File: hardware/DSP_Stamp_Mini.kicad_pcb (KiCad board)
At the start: 2 copper layers, 37.5 x 62 mm, 73 parts, among them J1 Conn_01x10, J2 SM03B-SRSS-TB, J3 Conn_01x05, J4 USB_C_Receptacle_USB2.0_14P, J6 Conn_01x10, J7 Conn_01x02, J8 Conn_01x04, SW1 SW_Push, SW2 SW_Push, U1 RP2350_80QFN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

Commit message: repo cleanup
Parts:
- removed J3: Conn_01x05, Connector_PinHeader_2.54mm:PinHeader_1x05_P2.54mm_Vertical_SMD_Pin1Right
- removed J6: Conn_01x10, Connector_PinHeader_2.54mm:PinHeader_1x10_P2.54mm_Vertical_SMD_Pin1Right
- removed J7: Conn_01x02, Connector_PinHeader_2.54mm:PinHeader_1x02_P2.54mm_Vertical_SMD_Pin1Right
- added J5: Conn_01x12, Connector_PinHeader_2.54mm:PinHeader_1x12_P2.54mm_Vertical, B.Cu at (93.8, 63.5)
- J1: value Conn_01x10 -> Conn_01x14; footprint Connector_PinHeader_2.54mm:PinHeader_1x10_P2.54mm_Vertical_SMD_Pin1Right -> Connector_PinHeader_2.54mm:PinHeader_1x14_P2.54mm_Vertical
- moved U6 35.7 mm to (117.5, 65.0)
- moved C26 35.7 mm to (121.1, 66.4)
- moved C27 35.7 mm to (114.1, 66.4)
- moved C28 35.7 mm to (123.1, 66.4)
- moved C29 35.7 mm to (112.1, 66.4)
- moved C30 35.7 mm to (125.1, 66.4)
- moved J1 19.9 mm to (129.3, 63.5), turned to 180 degrees
- moved R19 14.2 mm to (100.0, 99.9), turned to 90 degrees
- moved C21 13.7 mm to (121.0, 87.0), turned to -90 degrees
- moved D3 13.6 mm to (101.5, 99.9), turned to 90 degrees
- moved R18 13.6 mm to (104.5, 99.9), turned to 90 degrees
- moved D2 13.4 mm to (103.0, 99.9), turned to 90 degrees
- moved R13 12.0 mm to (125.5, 74.0), turned to 90 degrees
- moved D1 8.46 mm to (118.5, 59.5)
- moved R16 8.46 mm to (117.0, 59.5)
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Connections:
- J1 pad 2: /GPIO40_ADC0 -> /GPIO47_ADC7
- J1 pad 3: /GPIO41_ADC1 -> /GPIO46_ADC6
- J1 pad 4: /GPIO42_ADC2 -> /GPIO45_ADC5
- J1 pad 5: /GPIO43_ADC3 -> /GPIO44_ADC4
- J1 pad 6: /GPIO44_ADC4 -> /GPIO43_ADC3
- J1 pad 7: /GPIO45_ADC5 -> /GPIO42_ADC2
- J1 pad 8: /GPIO46_ADC6 -> /GPIO41_ADC1
- J1 pad 9: /GPIO47_ADC7 -> /GPIO40_ADC0
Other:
- board size 37.5 x 62 mm -> 39 x 54 mm

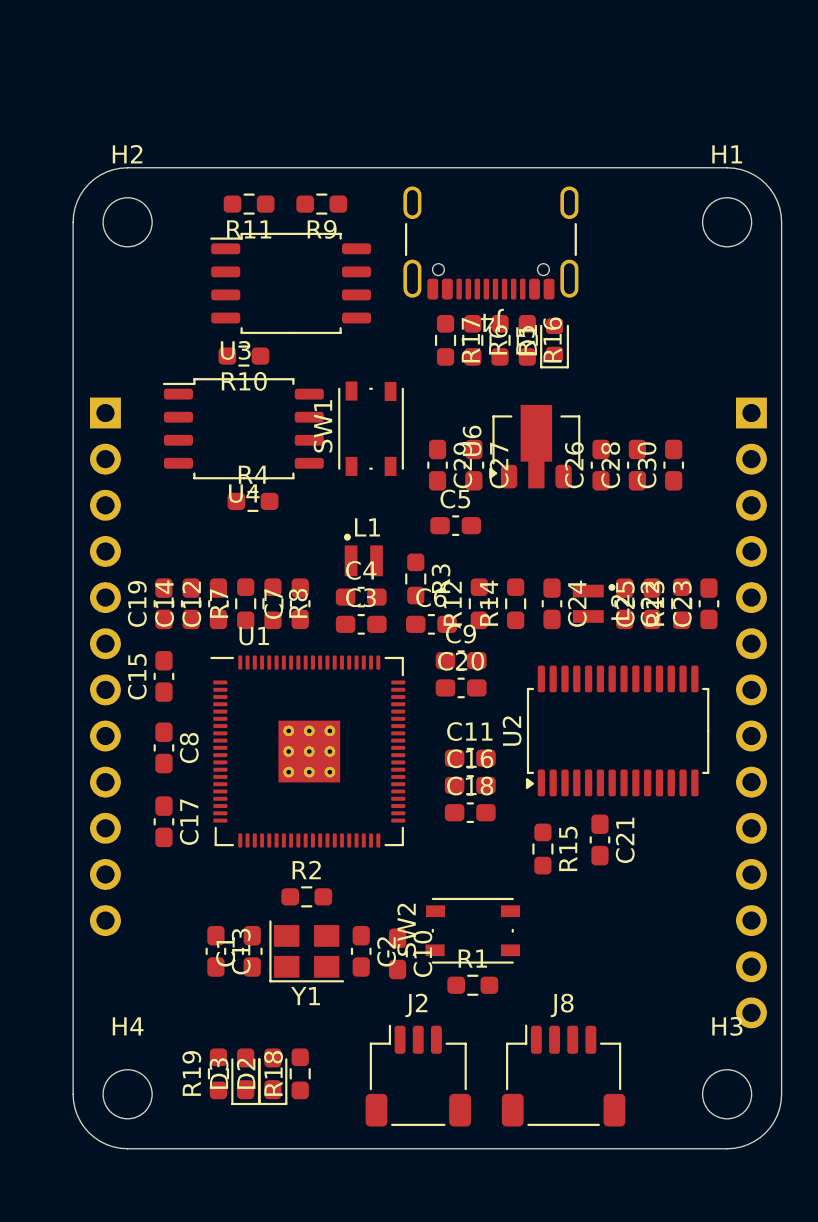
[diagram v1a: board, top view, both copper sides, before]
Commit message: change PCMxxx routing, partially route
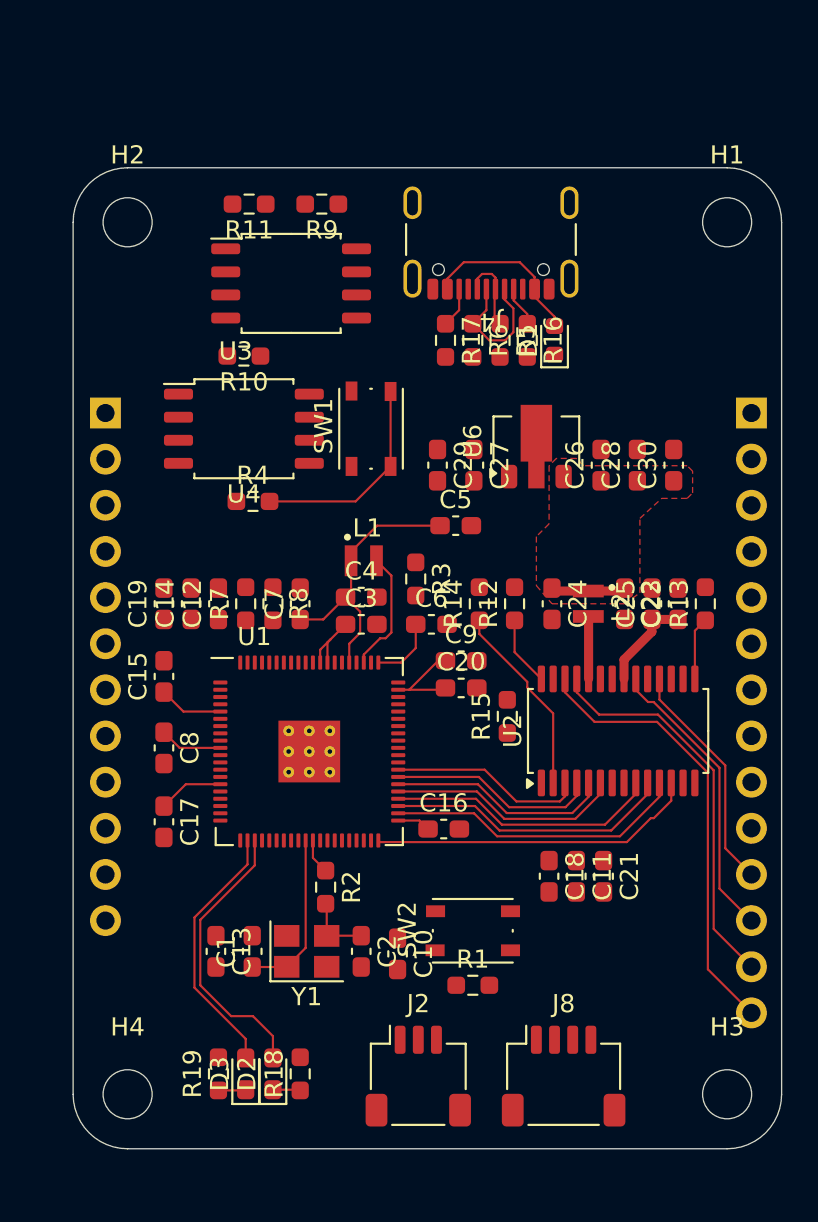
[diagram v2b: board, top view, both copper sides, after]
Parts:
- moved C11 8.74 mm to (119.7, 89.0), turned to -90 degrees
- moved R15 7.56 mm to (115.9, 80.2), turned to 90 degrees
- moved C18 5.57 mm to (118.2, 89.0), turned to -90 degrees
- moved C16 2.81 mm to (112.4, 86.4)
- moved C21 2.01 mm to (121.2, 89.0)
- moved R14 2.00 mm to (114.4, 74.0)
- moved R12 1.94 mm to (116.3, 74.0)
- moved C23 1.70 mm to (125.3, 74.0)
- moved R13 1.30 mm to (126.8, 74.0)
- moved R2 1.17 mm to (105.9, 89.6), turned to -90 degrees
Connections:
- J1 pad 13: /Vin_R -> /Vin_L
- J1 pad 14: /Vin_L -> /Vin_R
- U1 pad 40: /GPIO32 -> /DAC_DIN
- U1 pad 42: /GPIO33 -> /DAC_LRCLK
- U1 pad 43: /SDA -> /DAC_BCLK
- U1 pad 44: /SCL -> /DAC_SCLK
- U1 pad 45: /GPIO36 -> /ADC_SCLK
- U1 pad 46: /GPIO37 -> /ADC_BCLK
- U1 pad 47: /GPIO38 -> /ADC_LRCLK
- U1 pad 48: /GPIO39 -> /ADC_DIN
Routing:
- net /Vin_R: track 0.00 -> 24.7 mm
- net /Vin_L: track 0.00 -> 21.7 mm
- net +1V1: track 0.00 -> 18.8 mm
- net +3V3: track 0.00 -> 18.3 mm
- net /DAC_DIN: track 0.00 -> 18.1 mm
- net /DAC_LRCLK: track 0.00 -> 16.6 mm
- net /Vout_L: track 0.00 -> 16.1 mm
- net /DAC_BCLK: track 0.00 -> 15.7 mm
- net /GPIO23: track 0.00 -> 15.6 mm
- net /DAC_SCLK: track 0.00 -> 15.0 mm
- net /GPIO22: track 0.00 -> 14.3 mm
- net /ADC_SCLK: track 0.00 -> 12.9 mm
- net /Vout_R: track 0.00 -> 12.9 mm
- net /ADC_BCLK: track 0.00 -> 12.3 mm
- net /~{USB_BOOT}: track 0.00 -> 11.6 mm
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- added copper zone on F.Cu, net +5V
